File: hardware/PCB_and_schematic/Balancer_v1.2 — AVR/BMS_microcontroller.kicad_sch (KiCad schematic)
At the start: 59 parts, among them J10 RS485, J17 Conn_01x03, J2 ICP, J8 Conn_01x06, J9 RS485, Q23 BC817, U10 PC817, U11 LM7805_TO220, U12 LM317_TO-220, U4 TL432DBZ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

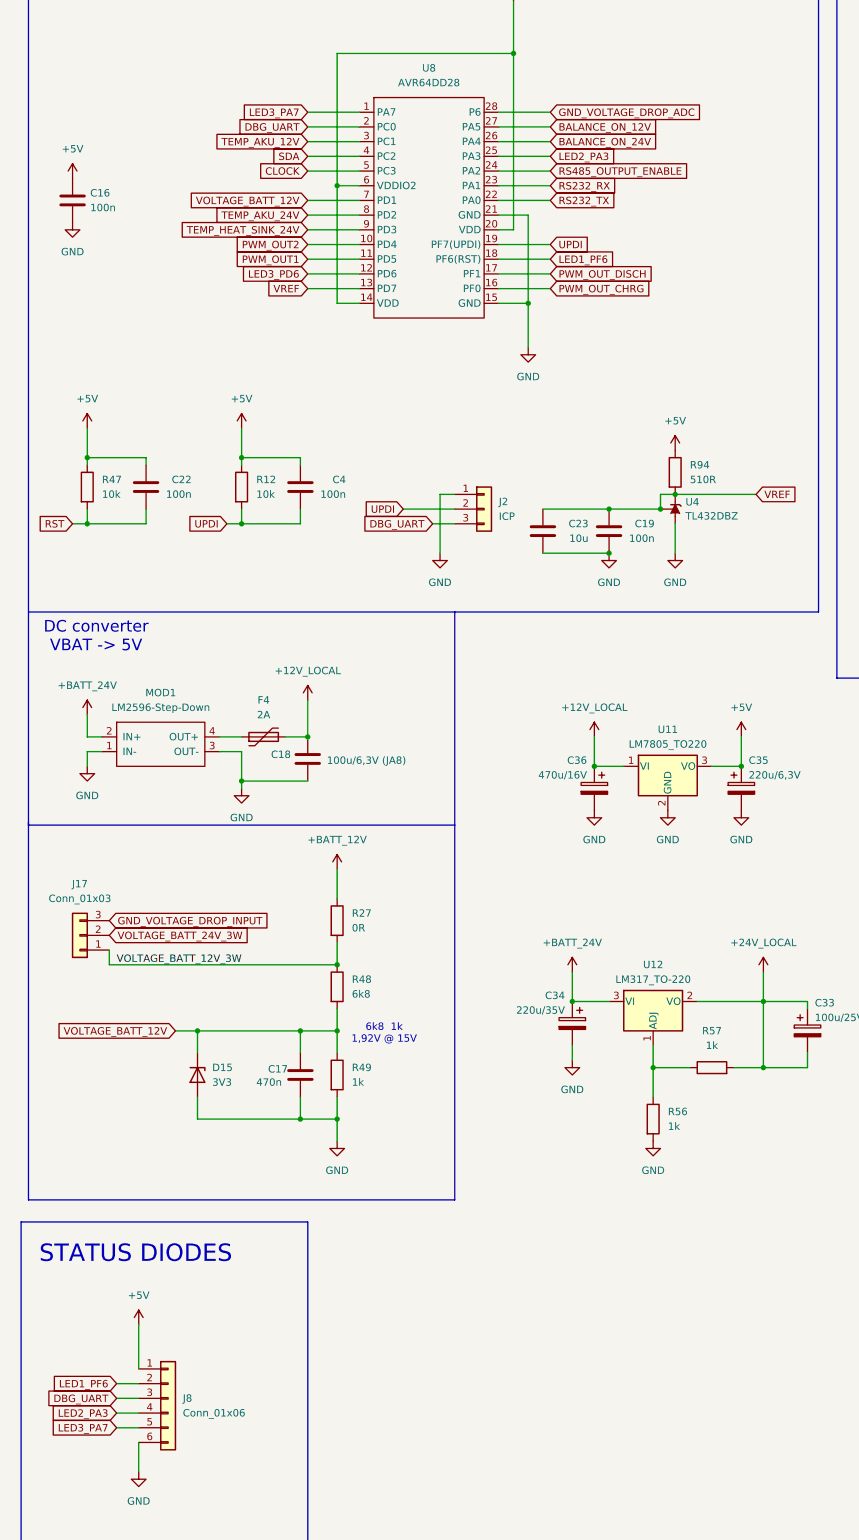
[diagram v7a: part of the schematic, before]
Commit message: mmc pinout update, change schematic
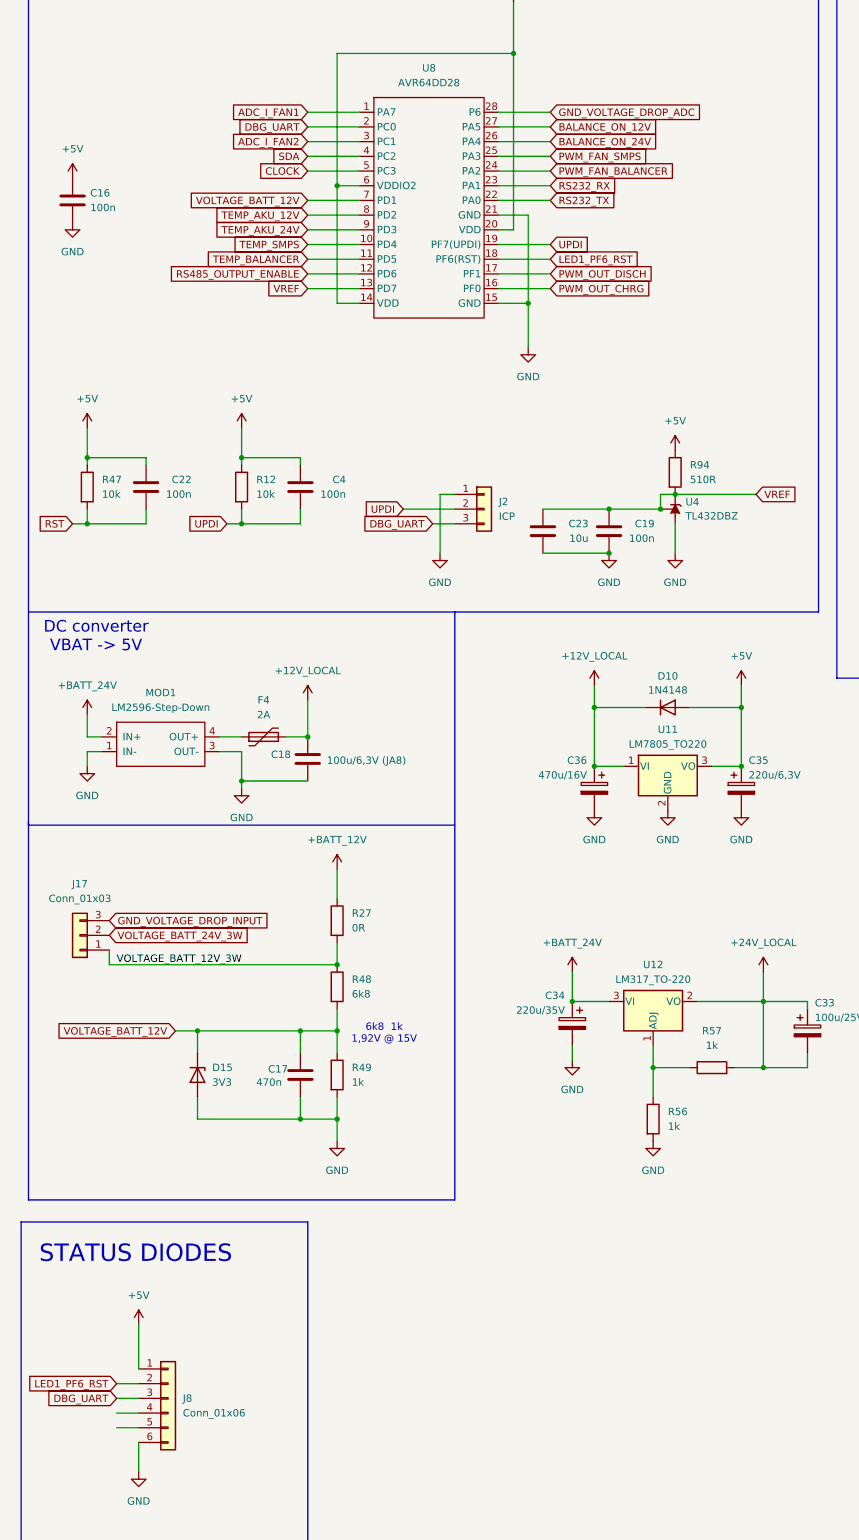
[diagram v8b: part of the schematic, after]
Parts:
- added D10: 1N4148, Diode_THT:D_DO-35_SOD27_P7.62mm_Horizontal, symbol Diode:1N4148
- J17: footprint (none) -> My-Footprints-connectors:JST_XA_1x03_P2.54mm_Vertical
- J2: footprint (none) -> Connector_PinHeader_2.54mm:PinHeader_1x03_P2.54mm_Vertical
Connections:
- net LED3_PD6 is gone; now on net RS485_OUTPUT_ENABLE: U8.12 (PD6)
- net TEMP_HEAT_SINK_24V is gone; now on net TEMP_AKU_24V: U8.9 (PD3)
- net +12V_LOCAL: now also D10.1 (K)
- net +5V: now also D10.2 (A)
- net RS485_OUTPUT_ENABLE: no longer U8.24 (PA2)
- net TEMP_AKU_12V: now also U8.8 (PD2); no longer U8.3 (PC1)
- net TEMP_AKU_24V: no longer U8.8 (PD2)
- net LED1_PF6 renamed LED1_PF6_RST
- net LED2_PA3: no longer names the net of J8.4 (Pin_4)
- net LED2_PA3: no longer U8.25 (PA3)
- net LED3_PA7: no longer names the net of J8.5 (Pin_5)
- net LED3_PA7: no longer U8.1 (PA7)
- net PWM_OUT1 renamed TEMP_BALANCER
- net PWM_OUT2 renamed TEMP_SMPS
- new net ADC_I_FAN1: U8.1 (PA7)
- new net ADC_I_FAN2: U8.3 (PC1)
- new net PWM_FAN_BALANCER: U8.24 (PA2)
- new net PWM_FAN_SMPS: U8.25 (PA3)
